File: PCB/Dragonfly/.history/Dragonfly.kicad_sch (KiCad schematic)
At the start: 28 parts, among them J1 Conn_01x04_Pin, SW1 SW_SPST, SW2 SW_SPST, U1 STM32F405RGTx, X1 TSX-3225

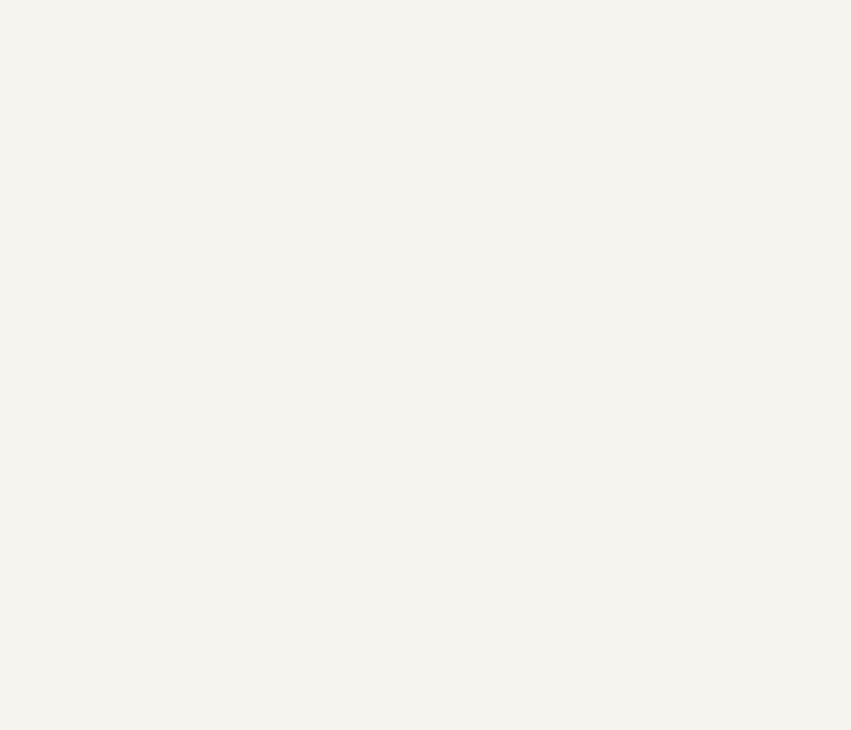
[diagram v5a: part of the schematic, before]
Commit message: Update Dragonfly.kicad_sch
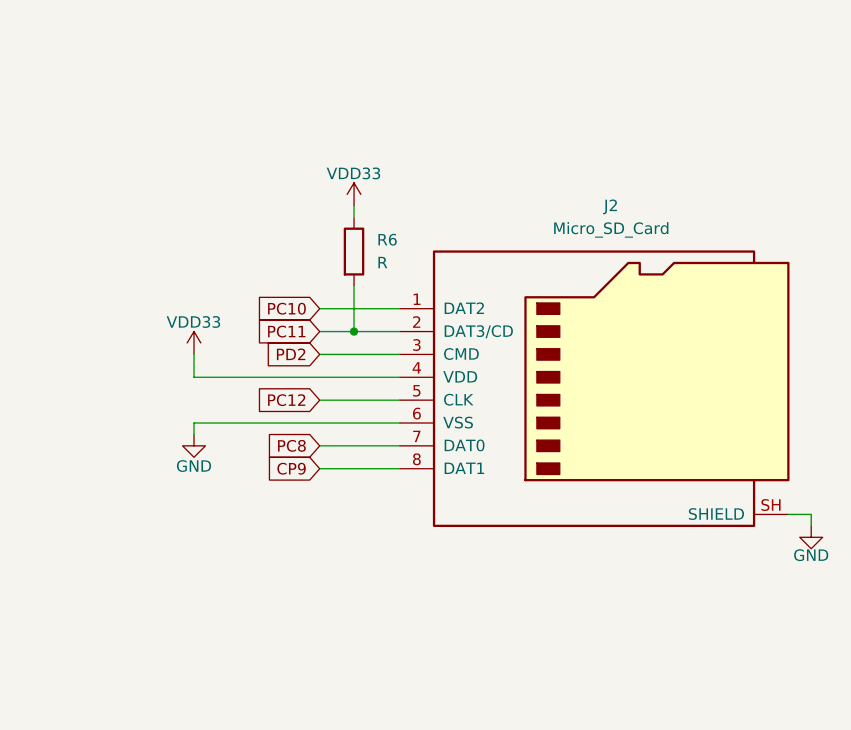
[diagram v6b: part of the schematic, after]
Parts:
- added J2: Micro_SD_Card, symbol Connector:Micro_SD_Card
- added R6: R, symbol Device:R
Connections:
- net CP9: now also J2.8 (DAT1)
- net GND: now also J2.6 (VSS), J2.SH (SHIELD)
- net PC10: now also J2.1 (DAT2)
- net PC11: now also J2.2 (DAT3/CD), R6.2
- net PC12: now also J2.5 (CLK)
- net PC8: now also J2.7 (DAT0)
- net PD2: now also J2.3 (CMD)
- net VDD33: now also J2.4 (VDD), R6.1

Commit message: Update Dragonfly.kicad_sch
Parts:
- added C15: 100nf, symbol Device:C
- added C16: 4.7uF, symbol Device:C
- added J3: USB_C_Receptacle_USB2.0_16P, symbol Connector:USB_C_Receptacle_USB2.0_16P
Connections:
- net GND: now also C15.2, C16.2
- net VDD33: now also C15.1, C16.1
- new net: J3.A1 (GND), J3.A12 (GND), J3.B1 (GND), J3.B12 (GND)
- new net: J3.A4 (VBUS), J3.A9 (VBUS), J3.B4 (VBUS), J3.B9 (VBUS)
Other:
- note added: "TF interface"
- moved on the sheet: J2, R6

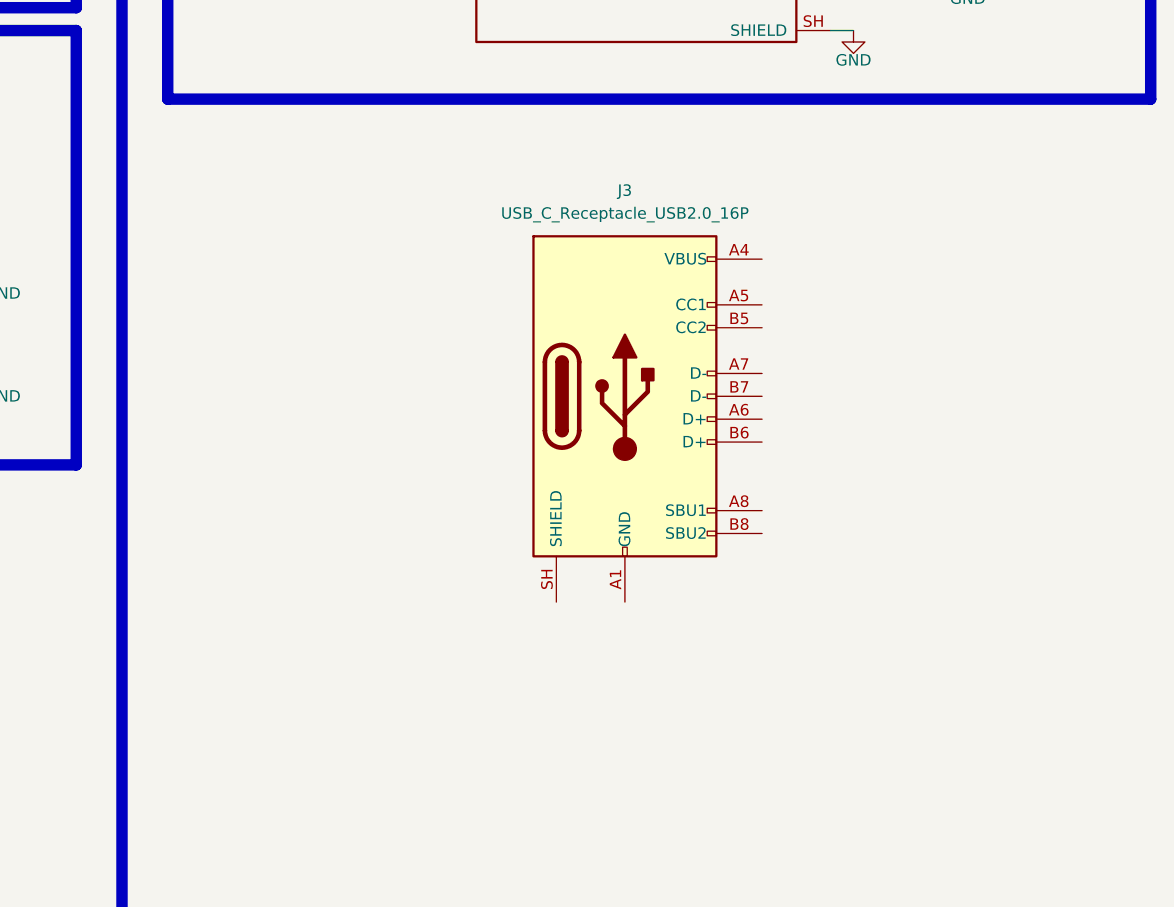
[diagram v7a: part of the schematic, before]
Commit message: Update Dragonfly.kicad_sch
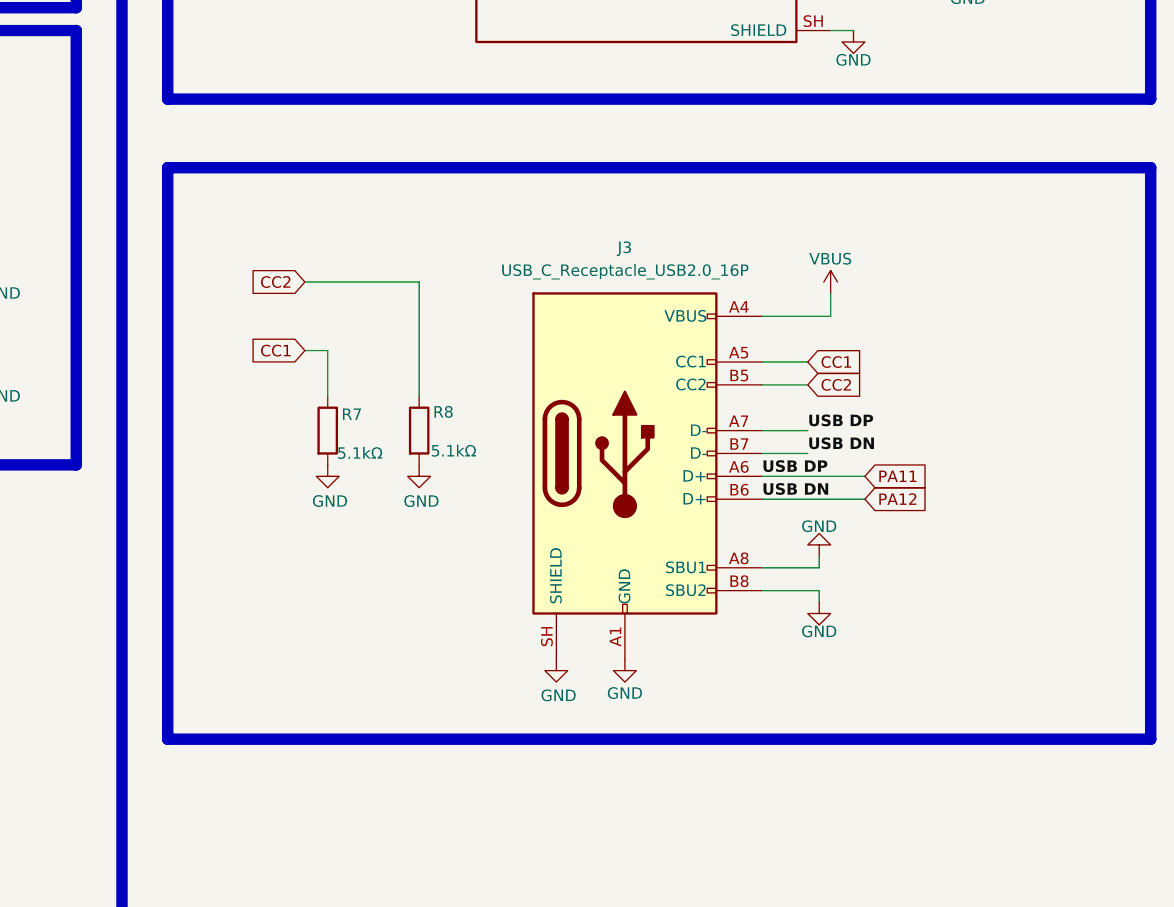
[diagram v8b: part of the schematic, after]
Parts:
- added R7, R8: 5.1kΩ, symbol Device:R
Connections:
- net GND: now also J3.A1 (GND), J3.A12 (GND), J3.A8 (SBU1), J3.B1 (GND), J3.B12 (GND), J3.B8 (SBU2), J3.SH (SHIELD), R7.2, R8.2
- net PA11: now also J3.A6 (D+), J3.A7 (D-)
- net PA12: now also J3.B6 (D+), J3.B7 (D-)
- net VBUS: now reaches J3.A4 (VBUS), J3.A9 (VBUS), J3.B4 (VBUS), J3.B9 (VBUS)
- net CC1: now reaches J3.A5 (CC1)
- net CC1: now also R7.1
- net CC2: now reaches J3.B5 (CC2)
- net CC2: now also R8.1
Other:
- moved on the sheet: J3
